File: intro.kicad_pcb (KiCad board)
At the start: 2 copper layers, 148.5 x 110.1 mm, 131 parts, among them IC1 IS31FL3741A-QFLS4-TR, IC2 IS31FL3741A-QFLS4-TR, SW1 SW_Push, SW10 SW_Push, SW11 SW_Push, SW12 SW_Push, SW13 SW_Push, SW14 SW_Push, SW15 SW_Push, SW16 SW_Push, SW17 SW_Push, SW18 SW_Push, SW19 SW_Push, SW2 SW_Push, SW20 SW_Push, SW21 SW_Push, SW22 SW_Push, SW23 SW_Push, SW24 SW_Push, SW25 SW_Push, SW26 SW_Push, SW27 SW_Push, SW28 SW_Push, SW29 SW_Push, SW3 SW_Push, SW30 SW_Push, SW31 SW_Push, SW32 SW_Push, SW33 SW_Push, SW34 SW_Push, SW35 RotaryEncoder_Switch, SW4 SW_Push, SW5 SW_Push, SW6 SW_Push, SW7 SW_Push, SW8 SW_Push, SW9 SW_Push, U1 nice_nano

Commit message: WIP: Additonal progress
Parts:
- moved IC2 50.9 mm to (195.6, 107.7)
- moved IC1 1.72 mm to (178.1, 107.5)
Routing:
- net CS1: track 43.3 -> 158.3 mm, vias 3 -> 4
- net CS8: track 43.1 -> 156.3 mm, vias 3 -> 5
- net CS9: track 52.4 -> 151.9 mm, vias 4 -> 6
- net CS15: track 5.72 -> 101.7 mm, vias 4 -> 5
- net CS2: track 45.3 -> 134.1 mm, vias 3 -> 5
- net CS10: track 52.2 -> 131.5 mm, vias 4 -> 6
- net CS16: track 5.72 -> 80.9 mm, vias 4 -> 6
- net CS3: track 46.3 -> 116.2 mm, vias 4 -> 6
- net CS11: track 52.5 -> 112.7 mm, vias 4 -> 6
- net CS7: track 5.72 -> 63.8 mm, vias 4 -> 6
- net CS17: track 5.72 -> 63.4 mm, vias 4 -> 6
- net CS13: track 51.0 -> 107.3 mm, vias 4 -> 8
- net RSW3: track 385.1 -> 436.6 mm, vias 51 -> 56
- net CS4: track 46.5 -> 96.0 mm, vias 4 -> 6
- net RSW1: track 342.7 -> 390.7 mm, vias 18 -> 22
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
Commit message: Progress
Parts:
- moved IC2 14.7 mm to (180.9, 107.6)
- moved IC1 2.80 mm to (180.9, 107.6)
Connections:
- IC1 pad 26: CS1 -> unconnected-(IC1-Pad26)
- IC1 pad 27: CS2 -> unconnected-(IC1-Pad27)
- IC1 pad 28: CS3 -> unconnected-(IC1-Pad28)
- IC1 pad 29: CS4 -> unconnected-(IC1-Pad29)
- IC1 pad 30: CS5 -> unconnected-(IC1-Pad30)
- IC1 pad 31: CS7 -> unconnected-(IC1-Pad31)
- IC1 pad 32: CS6 -> unconnected-(IC1-Pad32)
- IC1 pad 33: CS14 -> unconnected-(IC1-Pad33)
- IC1 pad 34: CS13 -> unconnected-(IC1-Pad34)
- IC1 pad 35: CS12 -> unconnected-(IC1-Pad35)
- IC1 pad 37: CS11 -> unconnected-(IC1-Pad37)
- IC1 pad 38: CS10 -> unconnected-(IC1-Pad38)
- IC1 pad 39: CS9 -> unconnected-(IC1-Pad39)
- IC1 pad 40: CS8 -> CS14
- IC1 pad 41: CS18 -> CS7
- IC1 pad 42: CS17 -> CS6
- IC1 pad 43: CS16 -> CS1
- IC1 pad 44: CS15 -> CS2
- IC1 pad 45: CS19 -> CS3
- IC1 pad 46: CS20 -> CS5
- IC1 pad 47: unconnected-(IC1-Pad47) -> CS4
- IC1 pad 48: unconnected-(IC1-Pad48) -> CS13
- IC1 pad 49: unconnected-(IC1-Pad49) -> CS12
- IC1 pad 50: unconnected-(IC1-Pad50) -> CS11
- IC1 pad 51: unconnected-(IC1-Pad51) -> CS10
- IC1 pad 52: unconnected-(IC1-Pad52) -> CS9
- IC1 pad 53: unconnected-(IC1-Pad53) -> CS8
- IC1 pad 54: unconnected-(IC1-Pad54) -> CS15
- IC1 pad 56: unconnected-(IC1-Pad56) -> CS16
- IC1 pad 57: unconnected-(IC1-Pad57) -> CS17
- IC1 pad 58: unconnected-(IC1-Pad58) -> CS18
- IC1 pad 59: unconnected-(IC1-Pad59) -> CS19
- IC1 pad 60: unconnected-(IC1-Pad60) -> CS20
- IC2 pad 29: CS4 -> CS20
- IC2 pad 30: CS5 -> CS19
- IC2 pad 45: CS19 -> unconnected-(IC2-Pad45)
- IC2 pad 46: CS20 -> unconnected-(IC2-Pad46)
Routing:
- net RSW4: track 295.3 -> 343.1 mm, vias 17 -> 23
- net RSW6: track 330.4 -> 378.1 mm
- net CS15: track 101.7 -> 148.0 mm
- net RSW5: track 288.3 -> 334.0 mm, vias 17 -> 23
- net CS16: track 80.9 -> 125.3 mm
- net CS17: track 63.4 -> 105.9 mm
- net CS20: track 1.91 -> 26.7 mm, vias 1 -> 3
- net CS4: track 96.0 -> 112.2 mm, vias 6 -> 7
- net CS5: track 79.0 -> 93.2 mm, vias 4 -> 5
- net CS7: track 63.8 -> 76.1 mm, vias 6 -> 7
- net CS18: track 31.4 -> 43.4 mm
- net CS6: track 92.3 -> 104.1 mm, vias 6 -> 7
- net CS1: track 158.3 -> 169.8 mm, vias 4 -> 5
- net CS2: track 134.1 -> 145.4 mm, vias 5 -> 6
- net CS3: track 116.2 -> 127.3 mm, vias 6 -> 7
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
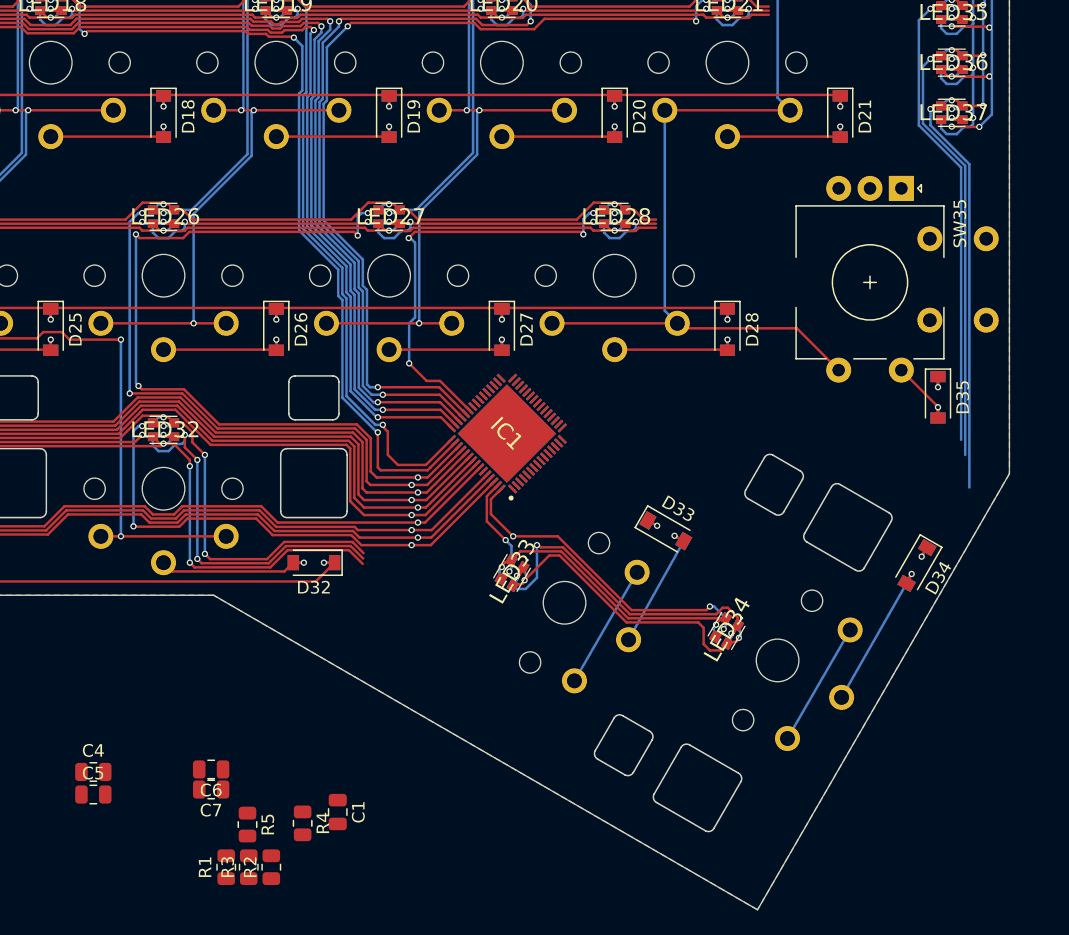
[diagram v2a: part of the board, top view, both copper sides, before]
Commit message: Add front-side SMD C/D/R
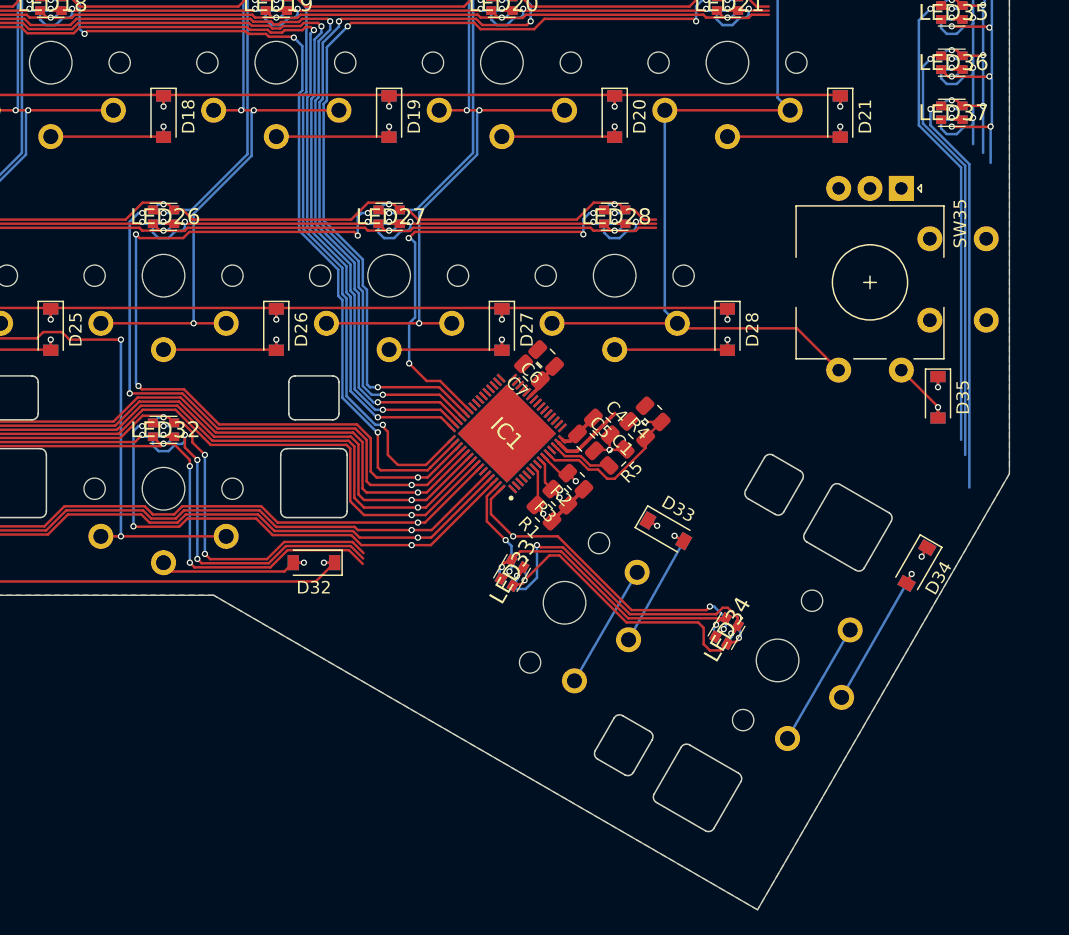
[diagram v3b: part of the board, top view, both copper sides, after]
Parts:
- moved C4 49.1 mm to (188.5, 107.0), turned to -45 degrees
- moved C5 48.3 mm to (187.2, 108.3), turned to -45 degrees
- moved R4 43.0 mm to (192.6, 106.0), turned to 135 degrees
- moved C6 42.3 mm to (184.0, 101.6), turned to 135 degrees
- moved C7 42.0 mm to (182.9, 102.7), turned to 135 degrees
- moved R5 41.6 mm to (189.7, 109.5), turned to -135 degrees
- moved R2 39.2 mm to (186.4, 111.4), turned to 135 degrees
- moved C1 38.7 mm to (191.3, 107.3), turned to 135 degrees
- moved R3 38.6 mm to (185.1, 112.7), turned to 135 degrees
- moved R1 38.0 mm to (183.9, 113.9), turned to 135 degrees
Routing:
- net VCC: track 0.00 -> 16.0 mm
- net SDB: track 0.00 -> 13.5 mm, vias 0 -> 1
- net Net-(IC1-Pad13): track 0.00 -> 4.93 mm
- net INTB: track 0.00 -> 4.12 mm, vias 0 -> 1
- net RSW5: track 334.0 -> 337.8 mm
- net GND: track 0.00 -> 3.74 mm, vias 0 -> 1
- net SDA: track 0.00 -> 3.56 mm, vias 0 -> 1
- net RSW4: track 343.1 -> 346.5 mm
- net SCL: track 0.00 -> 3.31 mm, vias 0 -> 1
- net RSW6: track 378.1 -> 380.2 mm

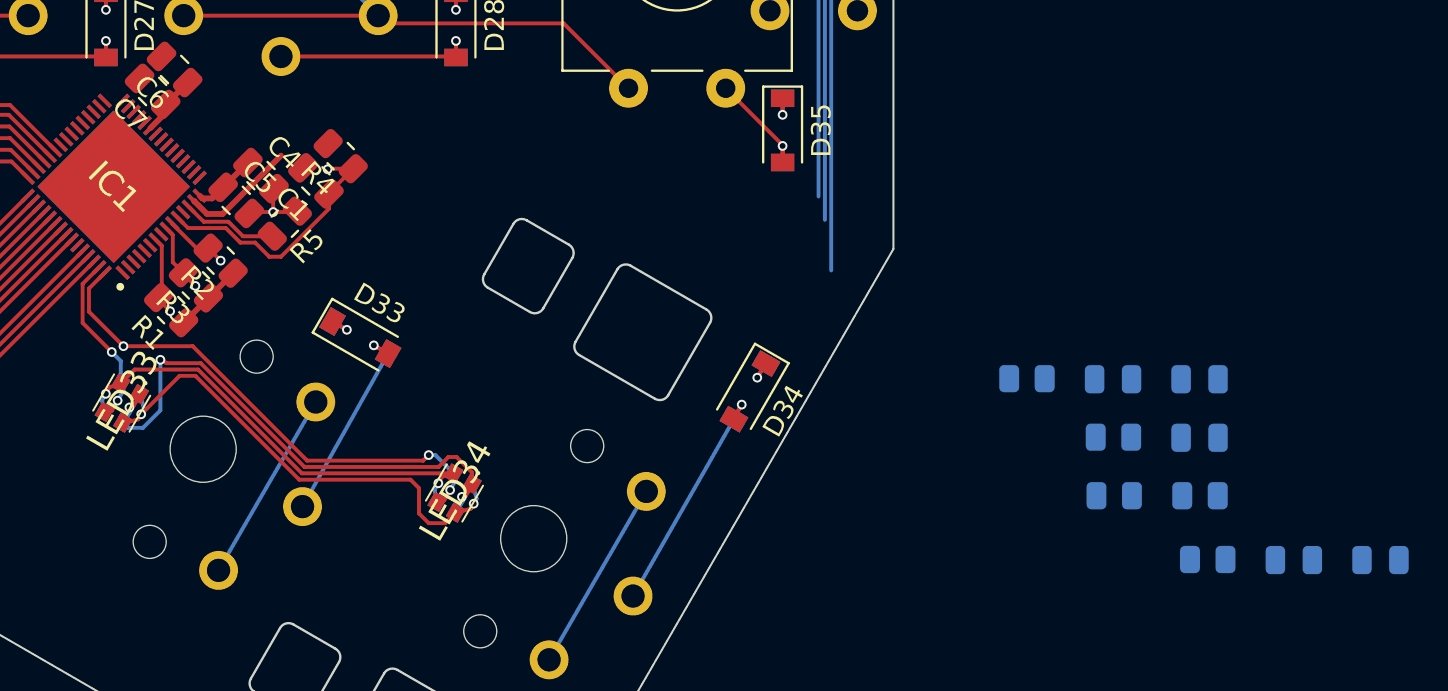
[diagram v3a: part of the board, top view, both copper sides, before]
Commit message: Start rear-side CMD C/D/R
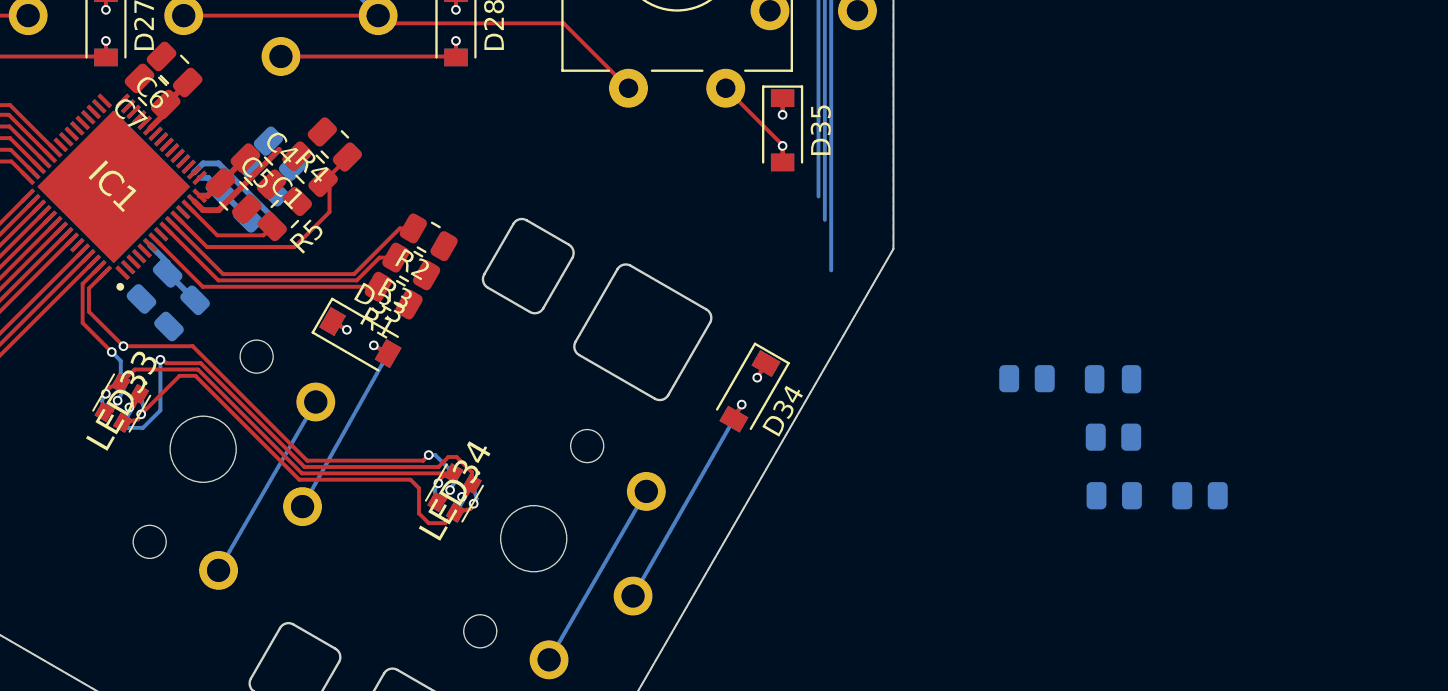
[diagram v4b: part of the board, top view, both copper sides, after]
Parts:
- moved C9 62.9 mm to (184.4, 114.1), turned to -135 degrees
- moved C3 56.2 mm to (188.5, 108.5), turned to 45 degrees
- moved C10 54.3 mm to (183.0, 112.7), turned to -135 degrees
- moved R10 52.0 mm to (189.5, 105.9), turned to 135 degrees
- moved C8 50.8 mm to (187.1, 107.1), turned to 45 degrees
- moved R1 11.5 mm to (195.3, 113.2), turned to 150 degrees
- moved R3 11.1 mm to (196.2, 111.7), turned to 150 degrees
- moved R2 10.8 mm to (197.1, 110.2), turned to 150 degrees
- moved R4 0.67 mm to (192.3, 105.4)
- moved C1 0.67 mm to (191.0, 106.7)
- moved R5 0.50 mm to (189.7, 109.0)
- moved C4 0.26 mm to (188.3, 106.8)
- moved C5 0.26 mm to (187.1, 108.1)
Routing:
- net SCL: track 3.31 -> 14.5 mm, vias 1 -> 0
- net SDA: track 3.56 -> 13.4 mm, vias 1 -> 0
- net VCC: track 16.0 -> 24.8 mm
- net INTB: track 4.12 -> 12.5 mm, vias 1 -> 0
- net GND: track 3.74 -> 0.00 mm, vias 1 -> 0
- net SDB: track 13.5 -> 12.7 mm, vias 1 -> 0
